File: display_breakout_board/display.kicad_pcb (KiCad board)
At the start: 2 copper layers, 26 x 34 mm, 9 parts, among them J1 541324562, J2 541324562, J3 Conn_02x12_Odd_Even, U1 MCP1664T-E/OT

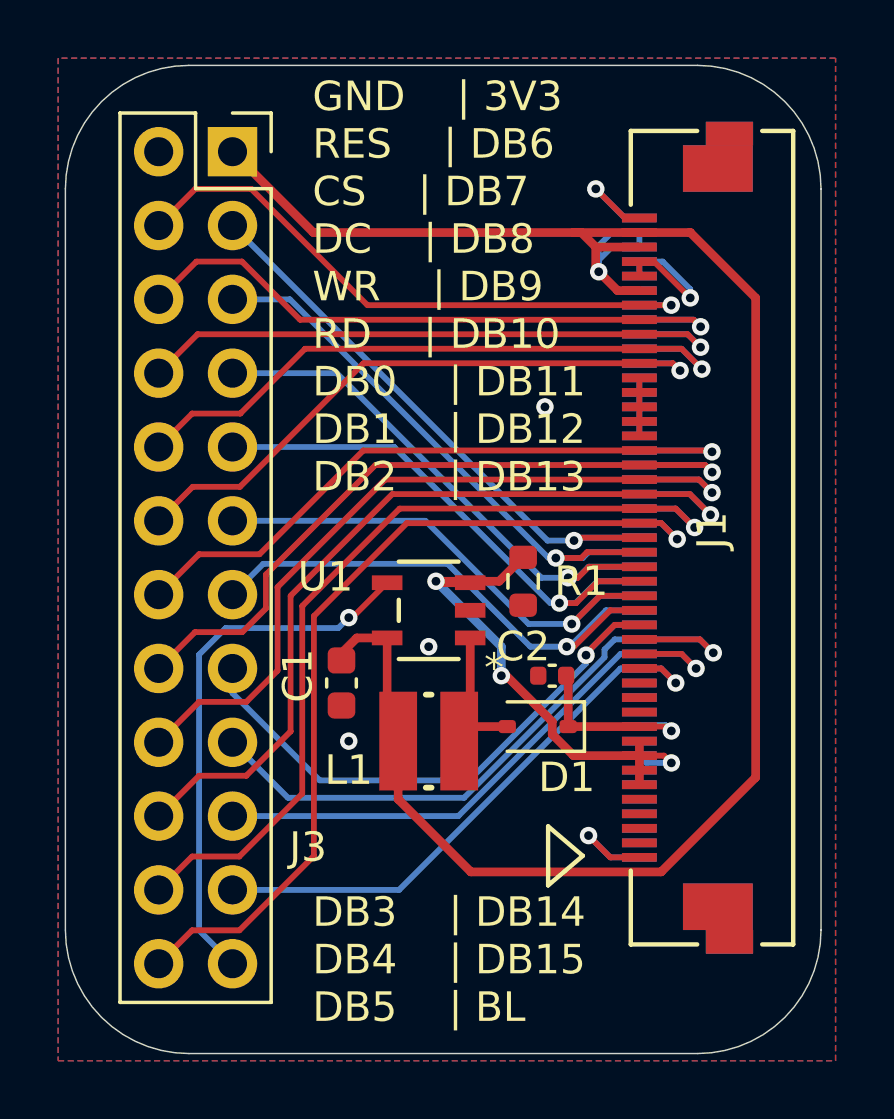
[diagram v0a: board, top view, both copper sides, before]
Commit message: Complete STM32H723ZGI6 144-pin schematic and FMC mapping
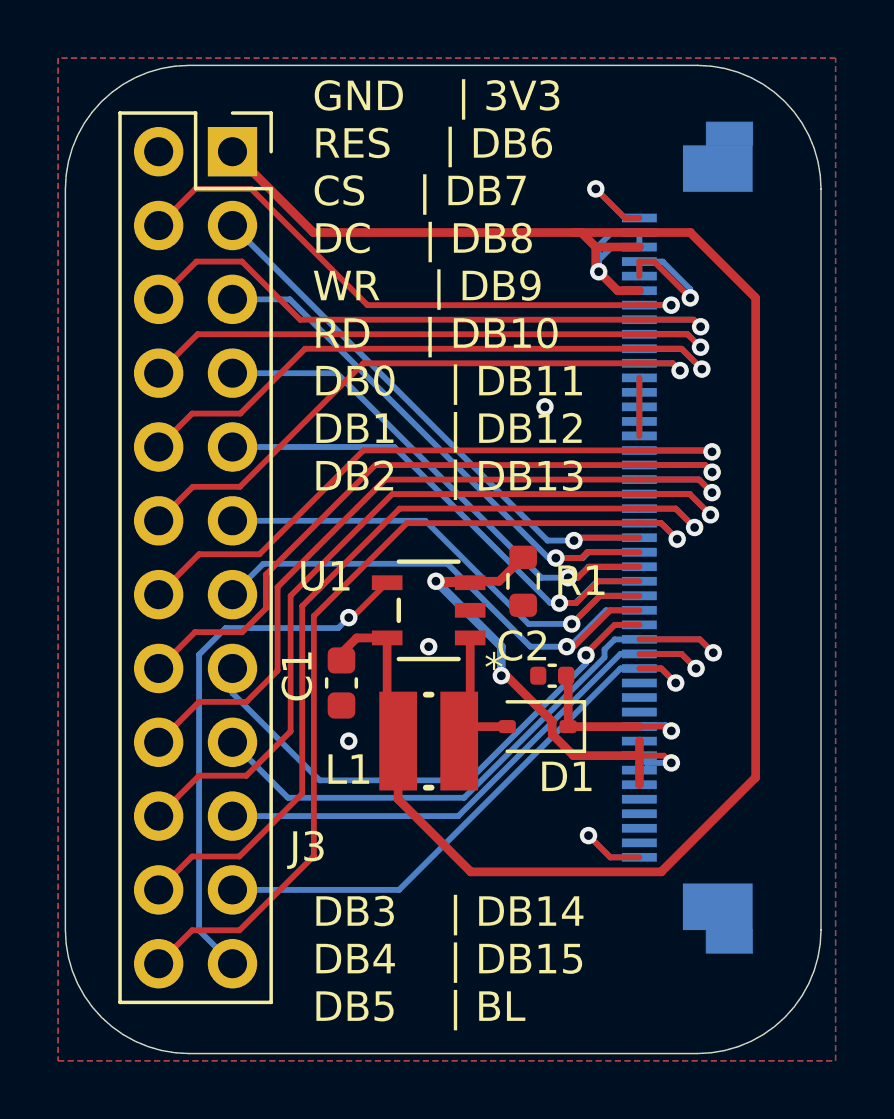
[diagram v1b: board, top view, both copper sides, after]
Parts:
- removed J1: 541324562, 541324562:CON_541324562_MOL

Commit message: Revert "Complete STM32H723ZGI6 144-pin schematic and FMC mapping"
This reverts commit c988dda79df5cbf87dce3ceded82a655262fe630.
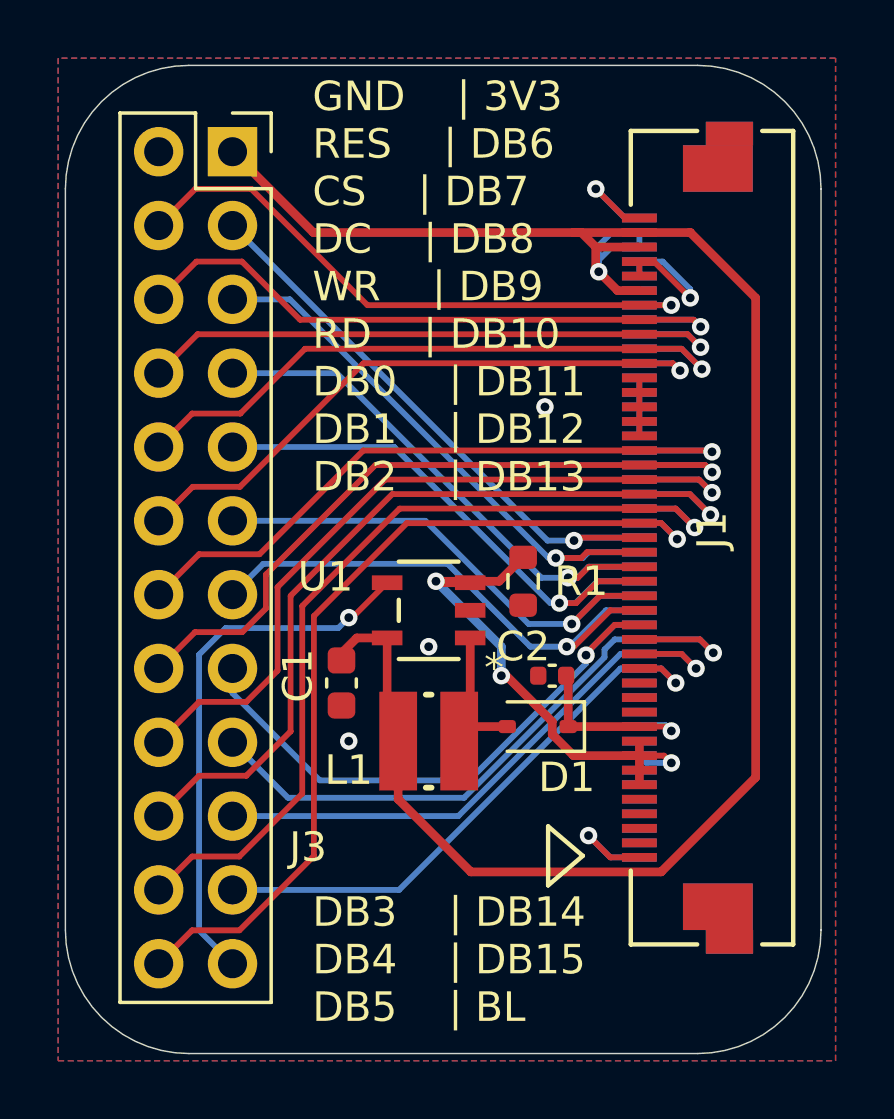
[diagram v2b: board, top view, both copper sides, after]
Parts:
- added J1: 541324562, 541324562:CON_541324562_MOL, F.Cu at (74.5, 55.3)
